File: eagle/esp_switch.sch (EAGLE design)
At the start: 14 parts, among them IC1 LT1117-3.3V

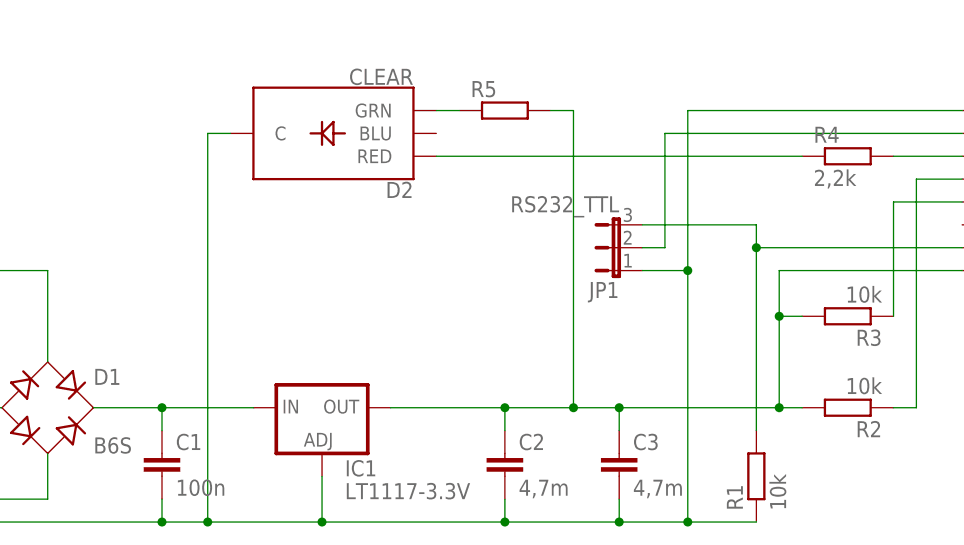
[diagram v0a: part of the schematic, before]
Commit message: add RGB LED
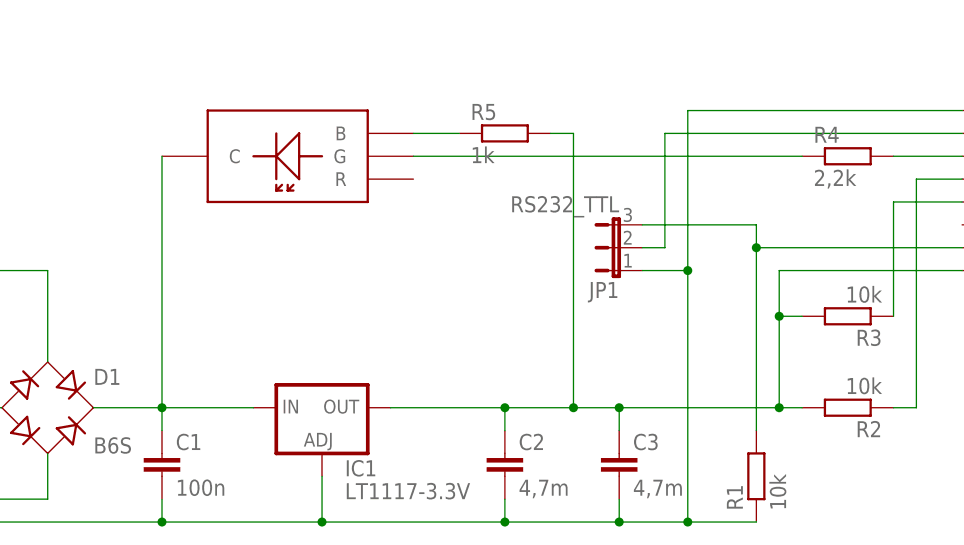
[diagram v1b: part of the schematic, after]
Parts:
- removed D2: CLEAR, SparkFun-LED:LED-RGB-CCCLEAR
- added U$1: RGB_LEDA, covek:RGB_LEDA
- R5: value (none) -> 1k
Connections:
- removed net N$13: D2.GRN, R5.1
- new net N$11: R5.1, U$1.B
- net N$12: now also U$1.G; no longer D2.RED
- net N$3: no longer D2.C
- net N$6: now also U$1.C
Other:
- moved on the sheet: R5
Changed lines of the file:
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@@
 <part name="R3" library="eagle-ltspice" deviceset="R" device="" value="10k"/>
 <part name="R4" library="eagle-ltspice" deviceset="R" device="" value="2,2k"/>
-<part name="D2" library="SparkFun-LED" deviceset="LED-RGB-CC" device="CLEAR" value="CLEAR"/>
-<part name="R5" library="eagle-ltspice" deviceset="R" device=""/>
+<part name="R5" library="eagle-ltspice" deviceset="R" device="" value="1k"/>
+<part name="U$1" library="covek" deviceset="RGB_LED" device="A"/>
 </parts>
 <sheets>
@@
 <instance part="R3" gate="G$1" x="162.56" y="93.98" rot="R180"/>
 <instance part="R4" gate="G$1" x="162.56" y="111.76"/>
-<instance part="D2" gate="G$1" x="106.68" y="114.3" rot="R180"/>
-<instance part="R5" gate="G$1" x="124.46" y="116.84"/>
+<instance part="R5" gate="G$1" x="124.46" y="114.3"/>
+<instance part="U$1" gate="G$1" x="99.06" y="114.3" rot="R180"/>
 </instances>
 <busses>
@@
 <wire x1="63.5" y1="83.82" x2="63.5" y2="71.12" width="0.1524" layer="91"/>
 <wire x1="63.5" y1="71.12" x2="86.36" y2="71.12" width="0.1524" layer="91"/>
-<wire x1="86.36" y1="71.12" x2="91.44" y2="71.12" width="0.1524" layer="91"/>
-<wire x1="91.44" y1="71.12" x2="104.14" y2="71.12" width="0.1524" layer="91"/>
+<wire x1="86.36" y1="71.12" x2="104.14" y2="71.12" width="0.1524" layer="91"/>
 <wire x1="104.14" y1="71.12" x2="124.46" y2="71.12" width="0.1524" layer="91"/>
 <wire x1="124.46" y1="71.12" x2="137.16" y2="71.12" width="0.1524" layer="91"/>
@@
 <wire x1="139.7" y1="99.06" x2="144.78" y2="99.06" width="0.1524" layer="91"/>
 <junction x="144.78" y="99.06"/>
-<pinref part="D2" gate="G$1" pin="C"/>
-<wire x1="93.98" y1="114.3" x2="91.44" y2="114.3" width="0.1524" layer="91"/>
-<wire x1="91.44" y1="114.3" x2="91.44" y2="71.12" width="0.1524" layer="91"/>
-<junction x="91.44" y="71.12"/>
 </segment>
 </net>
@@
 <wire x1="86.36" y1="81.28" x2="86.36" y2="83.82" width="0.1524" layer="91"/>
 <junction x="86.36" y="83.82"/>
+<wire x1="86.36" y1="83.82" x2="86.36" y2="111.76" width="0.1524" layer="91"/>
+<pinref part="U$1" gate="G$1" pin="C"/>
 </segment>
 </net>
@@
 <junction x="154.94" y="83.82"/>
 <pinref part="R5" gate="G$1" pin="2"/>
-<wire x1="129.54" y1="116.84" x2="132.08" y2="116.84" width="0.1524" layer="91"/>
-<wire x1="132.08" y1="116.84" x2="132.08" y2="83.82" width="0.1524" layer="91"/>
+<wire x1="129.54" y1="114.3" x2="132.08" y2="114.3" width="0.1524" layer="91"/>
+<wire x1="132.08" y1="114.3" x2="132.08" y2="83.82" width="0.1524" layer="91"/>
 <junction x="132.08" y="83.82"/>
 </segment>
@@
 </segment>
 </net>
+<net name="N$11" class="0">
+<segment>
+<pinref part="R5" gate="G$1" pin="1"/>
+<wire x1="114.3" y1="114.3" x2="119.38" y2="114.3" width="0.1524" layer="91"/>
+<pinref part="U$1" gate="G$1" pin="B"/>
+</segment>
+</net>
 <net name="N$12" class="0">
 <segment>
-<pinref part="D2" gate="G$1" pin="RED"/>
 <pinref part="R4" gate="G$1" pin="1"/>
-<wire x1="116.84" y1="111.76" x2="157.48" y2="111.76" width="0.1524" layer="91"/>
+<wire x1="114.3" y1="111.76" x2="157.48" y2="111.76" width="0.1524" layer="91"/>
+<pinref part="U$1" gate="G$1" pin="G"/>
 </segment>
 </net>
-<net name="N$13" class="0">
-<segment>
-<pinref part="D2" gate="G$1" pin="GRN"/>
-<pinref part="R5" gate="G$1" pin="1"/>
-<wire x1="116.84" y1="116.84" x2="119.38" y2="116.84" width="0.1524" layer="91"/>
-</segment>
-</net>

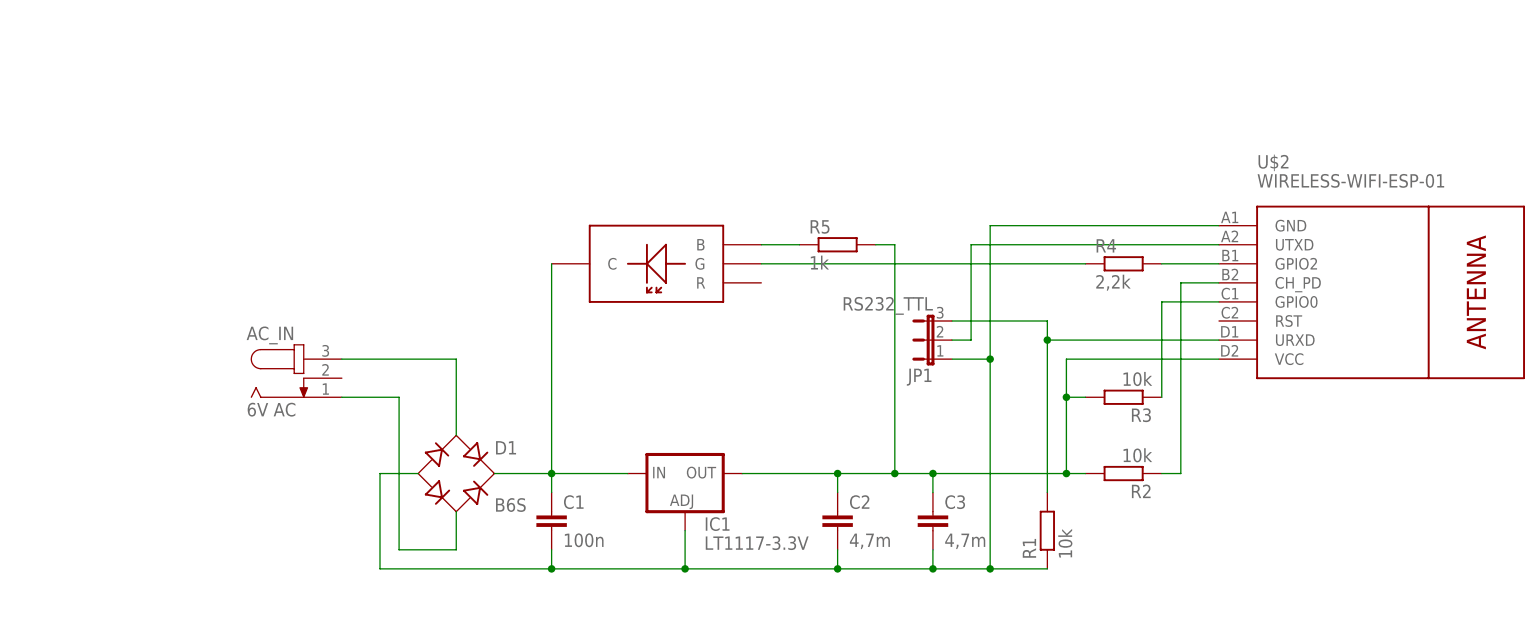
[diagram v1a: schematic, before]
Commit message: Add transistors and etc.
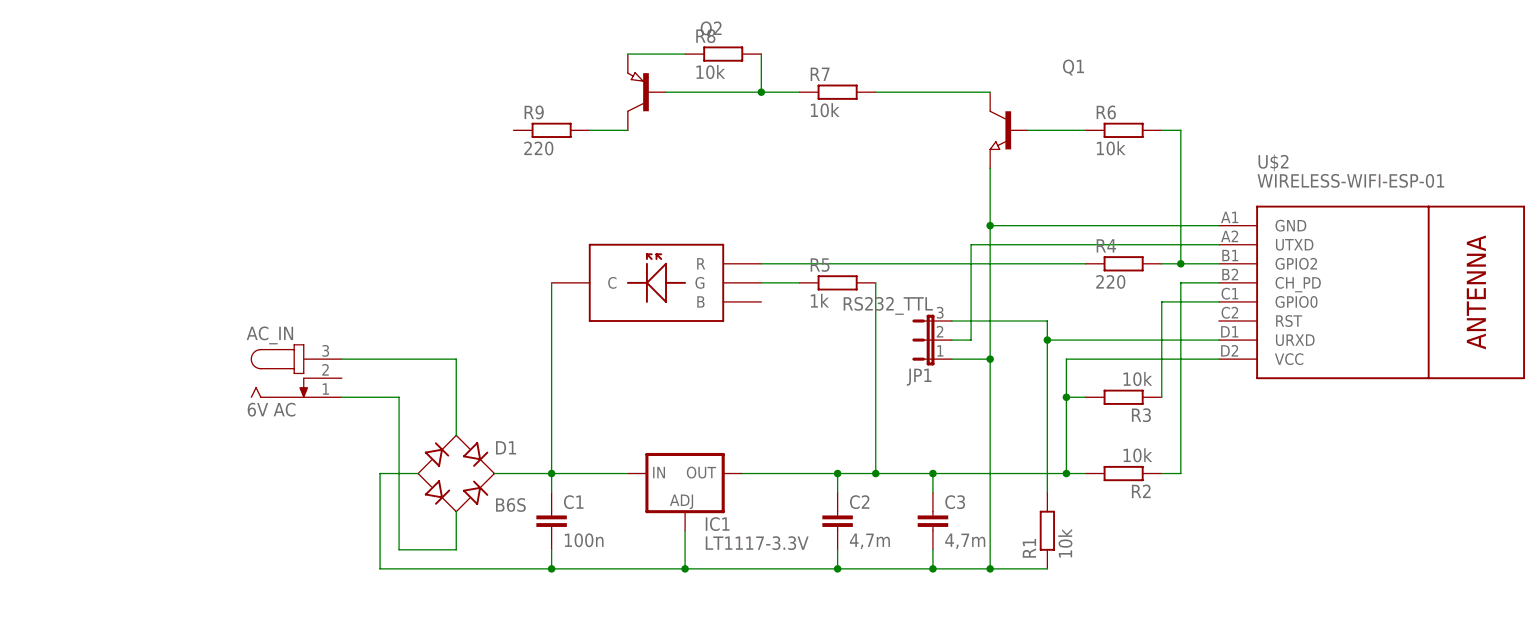
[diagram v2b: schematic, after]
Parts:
- added Q1: (no value), semicon-smd-ipc:NPN-TRANSISTOR_SOT23
- added Q2: (no value), semicon-smd-ipc:PNP-TRANSISTOR_SOT23
- added R6, R7, R8: 10k, eagle-ltspice:R
- added R9: 220, eagle-ltspice:R
- R4: value 2,2k -> 220
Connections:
- new net N$13: Q2.C, R9.2
- new net N$14: Q2.E, R8.1
- new net N$15: Q2.B, R7.1, R8.2
- new net N$16: Q1.C, R7.2
- new net N$17: Q1.B, R6.1
- net N$10: now also R6.2
- net N$11: now also U$1.G; no longer U$1.B
- net N$12: now also U$1.R; no longer U$1.G
- net N$3: now also Q1.E
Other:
- moved on the sheet: R5
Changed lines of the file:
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@@
 <?xml version="1.0" encoding="utf-8"?>
 <!DOCTYPE eagle SYSTEM "eagle.dtd">
-<eagle version="8.0.2">
+<eagle version="8.0.1">
 <drawing>
 <settings>
@@
 <part name="R2" library="eagle-ltspice" deviceset="R" device="" value="10k"/>
 <part name="R3" library="eagle-ltspice" deviceset="R" device="" value="10k"/>
-<part name="R4" library="eagle-ltspice" deviceset="R" device="" value="2,2k"/>
+<part name="R4" library="eagle-ltspice" deviceset="R" device="" value="220"/>
 <part name="R5" library="eagle-ltspice" deviceset="R" device="" value="1k"/>
+<part name="R6" library="eagle-ltspice" deviceset="R" device="" value="10k"/>
+<part name="R7" library="eagle-ltspice" deviceset="R" device="" value="10k"/>
+<part name="R8" library="eagle-ltspice" deviceset="R" device="" value="10k"/>
+<part name="R9" library="eagle-ltspice" deviceset="R" device="" value="220"/>
+<part name="Q1" library="semicon-smd-ipc" deviceset="NPN-TRANSISTOR_" device="SOT23"/>
+<part name="Q2" library="semicon-smd-ipc" deviceset="PNP-TRANSISTOR_" device="SOT23"/>
 <part name="U$1" library="covek" deviceset="RGB_LED" device="A"/>
 </parts>
@@
 <instance part="R3" gate="G$1" x="162.56" y="93.98" rot="R180"/>
 <instance part="R4" gate="G$1" x="162.56" y="111.76"/>
-<instance part="R5" gate="G$1" x="124.46" y="114.3"/>
-<instance part="U$1" gate="G$1" x="99.06" y="114.3" rot="R180"/>
+<instance part="R5" gate="G$1" x="124.46" y="109.22"/>
+<instance part="R6" gate="G$1" x="162.56" y="129.54"/>
+<instance part="R7" gate="G$1" x="124.46" y="134.62"/>
+<instance part="R8" gate="G$1" x="109.22" y="139.7"/>
+<instance part="R9" gate="G$1" x="86.36" y="129.54"/>
+<instance part="Q1" gate="G$1" x="147.32" y="129.54" rot="MR0"/>
+<instance part="Q2" gate="G$1" x="99.06" y="134.62" rot="MR0"/>
+<instance part="U$1" gate="G$1" x="99.06" y="106.68" rot="MR0"/>
 </instances>
 <busses>
@@
 <wire x1="139.7" y1="99.06" x2="144.78" y2="99.06" width="0.1524" layer="91"/>
 <junction x="144.78" y="99.06"/>
+<pinref part="Q1" gate="G$1" pin="E"/>
+<wire x1="144.78" y1="124.46" x2="144.78" y2="116.84" width="0.1524" layer="91"/>
+<junction x="144.78" y="116.84"/>
 </segment>
 </net>
@@
 <wire x1="86.36" y1="81.28" x2="86.36" y2="83.82" width="0.1524" layer="91"/>
 <junction x="86.36" y="83.82"/>
-<wire x1="86.36" y1="83.82" x2="86.36" y2="111.76" width="0.1524" layer="91"/>
+<wire x1="86.36" y1="83.82" x2="86.36" y2="109.22" width="0.1524" layer="91"/>
 <pinref part="U$1" gate="G$1" pin="C"/>
 </segment>
@@
 <pinref part="IC1" gate="G$1" pin="OUT"/>
 <wire x1="111.76" y1="83.82" x2="124.46" y2="83.82" width="0.1524" layer="91"/>
-<wire x1="124.46" y1="83.82" x2="132.08" y2="83.82" width="0.1524" layer="91"/>
+<wire x1="124.46" y1="83.82" x2="129.54" y2="83.82" width="0.1524" layer="91"/>
 <pinref part="C2" gate="G$1" pin="1"/>
-<wire x1="132.08" y1="83.82" x2="137.16" y2="83.82" width="0.1524" layer="91"/>
+<wire x1="129.54" y1="83.82" x2="137.16" y2="83.82" width="0.1524" layer="91"/>
 <wire x1="124.46" y1="81.28" x2="124.46" y2="83.82" width="0.1524" layer="91"/>
 <junction x="124.46" y="83.82"/>
@@
 <junction x="154.94" y="83.82"/>
 <pinref part="R5" gate="G$1" pin="2"/>
-<wire x1="129.54" y1="114.3" x2="132.08" y2="114.3" width="0.1524" layer="91"/>
-<wire x1="132.08" y1="114.3" x2="132.08" y2="83.82" width="0.1524" layer="91"/>
-<junction x="132.08" y="83.82"/>
+<wire x1="129.54" y1="109.22" x2="129.54" y2="83.82" width="0.1524" layer="91"/>
+<junction x="129.54" y="83.82"/>
 </segment>
 </net>
@@
 <pinref part="U$2" gate="G$1" pin="GPIO2"/>
 <pinref part="R4" gate="G$1" pin="2"/>
-<wire x1="175.26" y1="111.76" x2="167.64" y2="111.76" width="0.1524" layer="91"/>
+<wire x1="175.26" y1="111.76" x2="170.18" y2="111.76" width="0.1524" layer="91"/>
+<pinref part="R6" gate="G$1" pin="2"/>
+<wire x1="170.18" y1="111.76" x2="167.64" y2="111.76" width="0.1524" layer="91"/>
+<wire x1="167.64" y1="129.54" x2="170.18" y2="129.54" width="0.1524" layer="91"/>
+<wire x1="170.18" y1="129.54" x2="170.18" y2="111.76" width="0.1524" layer="91"/>
+<junction x="170.18" y="111.76"/>
 </segment>
 </net>
@@
 </segment>
 </net>
+<net name="N$13" class="0">
+<segment>
+<pinref part="R9" gate="G$1" pin="2"/>
+<pinref part="Q2" gate="G$1" pin="C"/>
+<wire x1="91.44" y1="129.54" x2="96.52" y2="129.54" width="0.1524" layer="91"/>
+</segment>
+</net>
+<net name="N$14" class="0">
+<segment>
+<pinref part="Q2" gate="G$1" pin="E"/>
+<pinref part="R8" gate="G$1" pin="1"/>
+<wire x1="96.52" y1="139.7" x2="104.14" y2="139.7" width="0.1524" layer="91"/>
+</segment>
+</net>
+<net name="N$15" class="0">
+<segment>
+<pinref part="Q2" gate="G$1" pin="B"/>
+<pinref part="R7" gate="G$1" pin="1"/>
+<wire x1="101.6" y1="134.62" x2="114.3" y2="134.62" width="0.1524" layer="91"/>
+<pinref part="R8" gate="G$1" pin="2"/>
+<wire x1="114.3" y1="134.62" x2="119.38" y2="134.62" width="0.1524" layer="91"/>
+<wire x1="114.3" y1="139.7" x2="114.3" y2="134.62" width="0.1524" layer="91"/>
+<junction x="114.3" y="134.62"/>
+</segment>
+</net>
+<net name="N$16" class="0">
+<segment>
+<pinref part="R7" gate="G$1" pin="2"/>
+<pinref part="Q1" gate="G$1" pin="C"/>
+<wire x1="129.54" y1="134.62" x2="144.78" y2="134.62" width="0.1524" layer="91"/>
+</segment>
+</net>
+<net name="N$17" class="0">
+<segment>
+<pinref part="Q1" gate="G$1" pin="B"/>
+<pinref part="R6" gate="G$1" pin="1"/>
+<wire x1="149.86" y1="129.54" x2="157.48" y2="129.54" width="0.1524" layer="91"/>
+</segment>
+</net>
 <net name="N$11" class="0">
 <segment>
+<pinref part="U$1" gate="G$1" pin="G"/>
 <pinref part="R5" gate="G$1" pin="1"/>
-<wire x1="114.3" y1="114.3" x2="119.38" y2="114.3" width="0.1524" layer="91"/>
-<pinref part="U$1" gate="G$1" pin="B"/>
+<wire x1="114.3" y1="109.22" x2="119.38" y2="109.22" width="0.1524" layer="91"/>
 </segment>
 </net>
 <net name="N$12" class="0">
 <segment>
+<pinref part="U$1" gate="G$1" pin="R"/>
 <pinref part="R4" gate="G$1" pin="1"/>
 <wire x1="114.3" y1="111.76" x2="157.48" y2="111.76" width="0.1524" layer="91"/>
-<pinref part="U$1" gate="G$1" pin="G"/>
-</segment>
-</net>
+</segment>
+</net>

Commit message: modified brd size for case and add out port,SSR to sch, brd
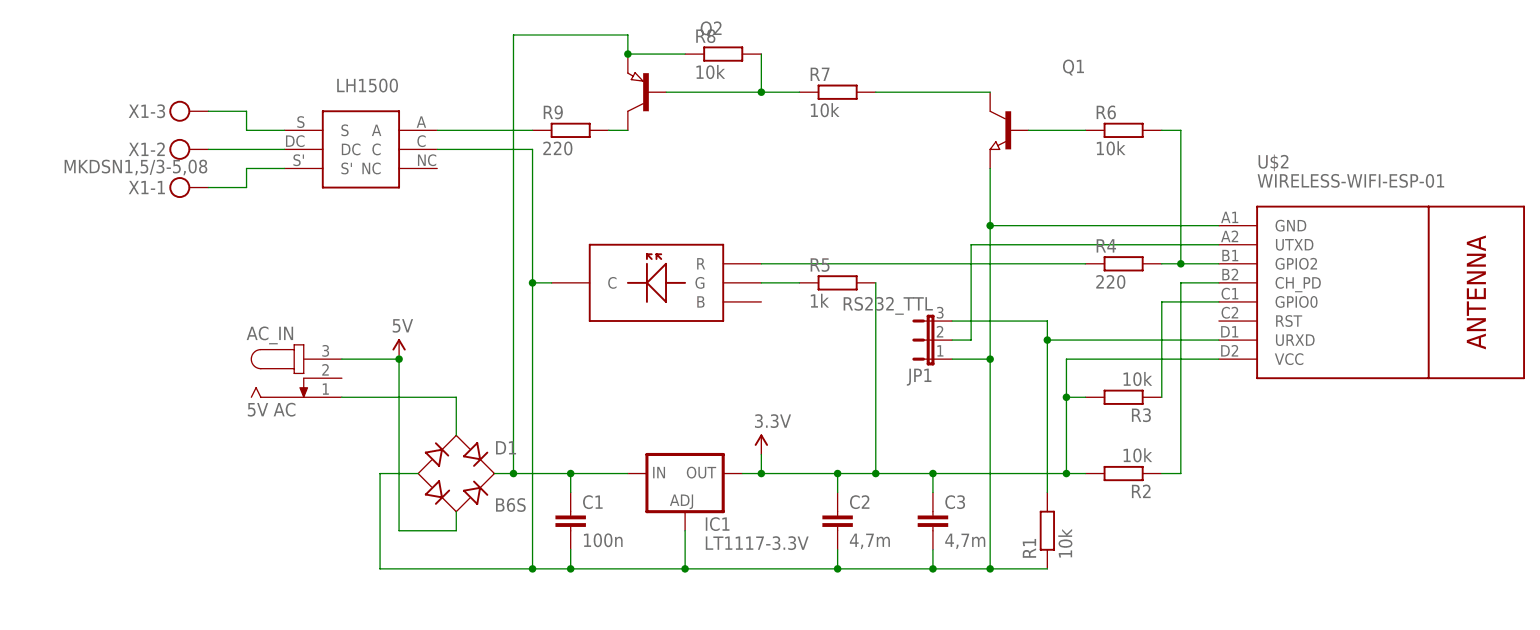
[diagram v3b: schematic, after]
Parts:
- added LH1500: (no value), LH1500:LH1500
- added X1: MKDSN1,5/3-5,08, con-phoenix-508:MKDSN1,5/3-5,08
- AC_IN: value 6V AC -> 5V AC
- renumbered U$1 to RGBLED5MM
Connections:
- net N$7 renamed 3.3V
- new net 5V: AC_IN.3, D1.AC2
- new net N$18: LH1500.A, R9.1
- new net N$7: LH1500.DC, X1-2.KL
- net N$1: now also D1.AC1; no longer D1.AC2
- net N$14: now also LH1500.S', X1-1.KL; no longer Q2.E, R8.1
- net N$2: now also LH1500.S, X1-3.KL; no longer AC_IN.3, D1.AC1
- net N$3: now also LH1500.C, RGBLED5MM.C
- net N$6: now also Q2.E, R8.1; no longer RGBLED5MM.C
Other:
- moved on the sheet: C1, R9
